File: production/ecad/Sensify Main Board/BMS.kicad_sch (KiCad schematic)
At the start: 0 parts

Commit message: rough draft for BMS schematic
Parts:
- added BT1, BT2: 3.7V, symbol Device:Battery_Cell
- added C1, C2, C3, C8: 0.47u, symbol Device:C
- added C10: 0.33u, symbol Device:C
- added C11: 10u, symbol Device:C_Polarized
- added C12: 470p, symbol Device:C
- added C13: 2.2u, symbol Device:C
- added C4, C6, C7: 0.01u, symbol Device:C
- added C5, C9: 0.1u, symbol Device:C
- added Q1, Q2, Q3: NMOS, symbol Simulation_SPICE:NMOS
- added R1: 5m, symbol Device:R_Shunt_US
- added R2: R_US, symbol Device:R_US
- added R3: 1k, symbol Device:R_US
- added R4, R5: 100, symbol Device:R_US
- added R6: 10k, symbol Device:R_US
- added R7, R8: 50, symbol Device:R_US
- added R9: 10, symbol Device:R_US
- added TH1: 10k, symbol Device:Thermistor_US
- added U1: MAX17320G22, MAX17320G22_:TQFN-24, symbol MAX17320G22_:MAX17320G22_
- added U2: LD29150DT33R, LD29150DT33R:DPAK456P972X240-3N, symbol LD29150DT33R:LD29150DT33R
- added U3: MIC5205-5.0YM5-TR, MIC5205-5.0YM5-TR:SOT95P280X145-5N, symbol MIC5205-5.0YM5-TR:MIC5205-5.0YM5-TR
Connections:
- new net: Q3.2 (G), R6.1, U1.11 (PFAIL)
- new net: C6.1, C7.2, R7.1, U1.21 (CELL1), U1.22 (CELL2), U1.23 (CELL3)
- new net: C5.1, Q1.1 (D)
- new net: C5.2, Q1.2 (G), R4.1
- new net: Q1.3 (S), Q2.1 (D)
- new net: C12.1, U3.4 (BYP)
- new net: C7.1, R8.1, U1.24 (BATTS)
- new net: R1.2, U1.15 (CSP)
- new net: R1.3, U1.14 (CSN)
- new net: R4.2, U1.3 (CHG)
- new net: BT1.2 (-), BT2.1 (+), R7.2
- new net: R2.2, U1.5 (ZVC)
- new net: TH1.2, U1.10 (TH1)
- new net: C1.1, U1.12 (AOLDO)
- new net: C3.1, U1.13 (REG3)
- new net: C2.1, U1.17 (REG2)
- new net: C8.1, U1.2 (CP)
- new net: R5.2, U1.4 (DIS)
- new net: C4.1, R3.2, U1.6 (PCKP)
- new net: U1.EP, U1.P$1 (EP), U1.P$2 (EP), U1.P$3 (EP), U1.P$4 (EP), U1.P$5 (EP)
- new net: Q2.2 (G), R5.1
- new net +3.3V: C11.1, U2.2 (OUTPUT)
- new net +5V: C13.1, U3.5 (OUT)
- new net GND: BT1.1 (+), BT2.2 (-), C1.2, C10.2, C11.2, C12.2, C13.2, C2.2, C3.2, C4.2, C6.2, C8.2, C9.1, C9.2, Q3.1 (D), R1.1, R6.2, R8.2, R9.1, R9.2, TH1.1, U1.1 (IN), U1.20 (GND), U2.3 (GND), U3.2 (GND)
- new net PACK+: C10.1, Q2.3 (S), R2.1, R3.1, U2.1 (INPUT), U3.1 (IN), U3.3 (EN)
- new net PACK-: R1.4
- new net SCL: U1.8 (SCL/OD)
- new net SDA: U1.9 (SDA/DQ)
- no-connect marks 0 -> 3
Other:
- note added: "3 terminal fuse"
- note added: "BMIC"
- note added: "Choose R"
- note added: "LDO (BATT->3.3V)"
- note added: "LDO (BATT->5V)"
- note added: "Tantalum"

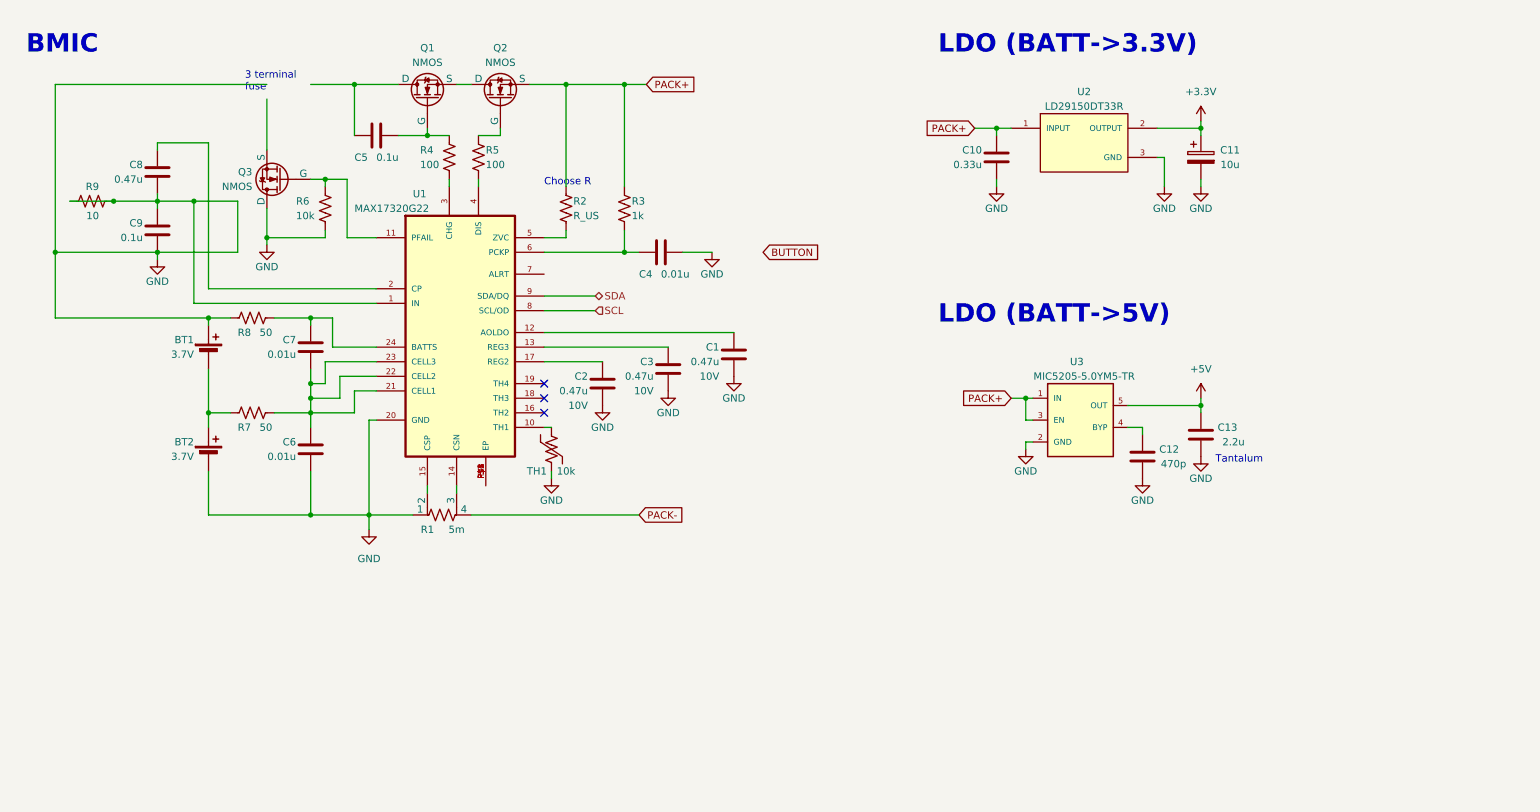
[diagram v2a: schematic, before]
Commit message: added to BMS schematic
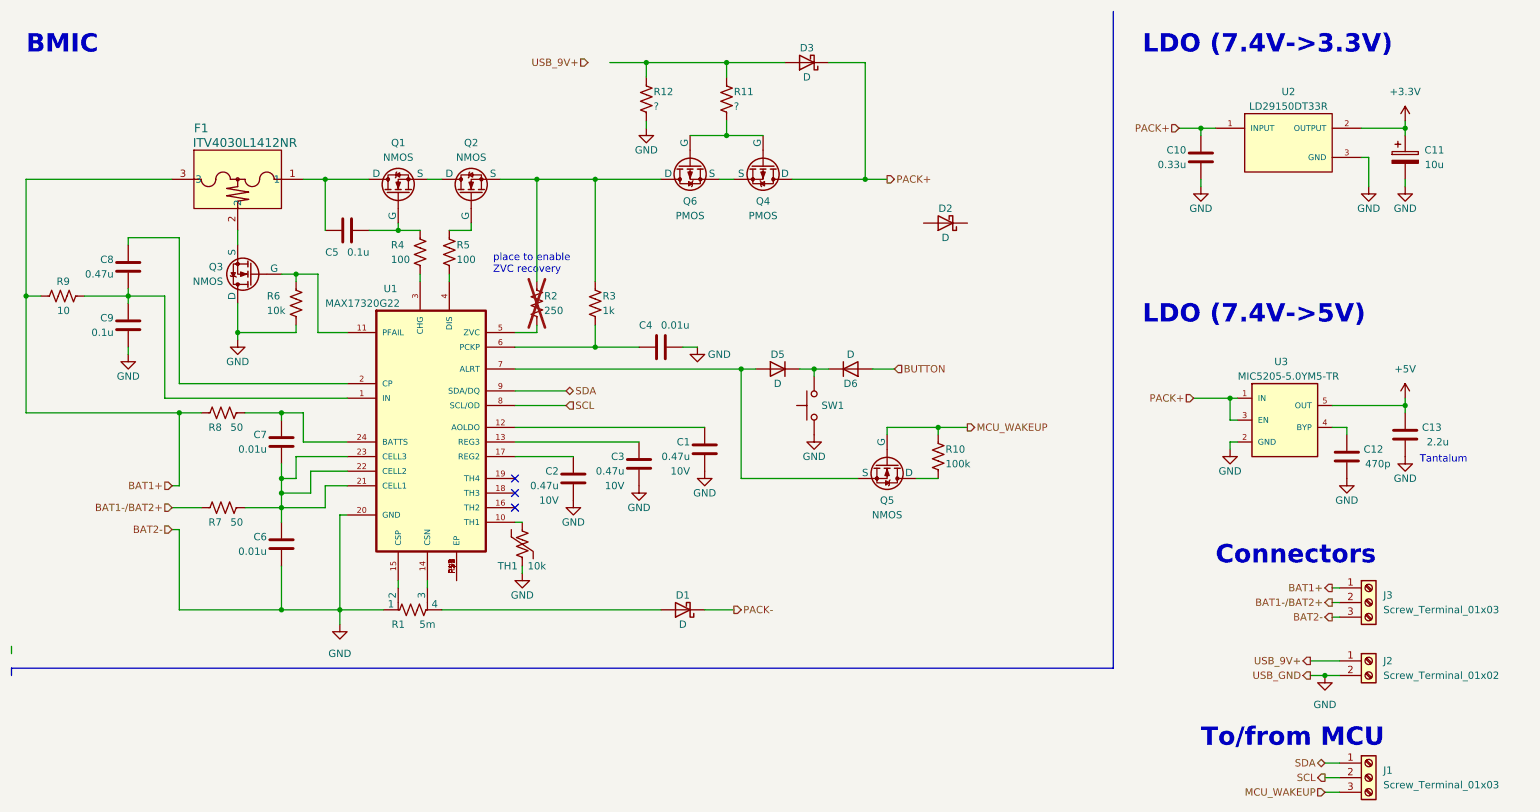
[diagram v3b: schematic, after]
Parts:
- removed BT1, BT2: 3.7V, symbol Device:Battery_Cell
- added D1, D2, D3: D, symbol Device:D_Schottky
- added D5, D6: D, symbol Device:D
- added F1: ITV4030L1412NR, BMS:ITV4030_LTF, symbol 2024-10-02_16-38-03:ITV4030L1412NR
- added J1, J3: Screw_Terminal_01x03, symbol Connector:Screw_Terminal_01x03
- added J2: Screw_Terminal_01x02, symbol Connector:Screw_Terminal_01x02
- added Q4, Q6: PMOS, symbol Simulation_SPICE:PMOS
- added Q5: NMOS, symbol Simulation_SPICE:NMOS
- added R10: 100k, symbol Device:R_US
- added R11, R12: ?, symbol Device:R_US
- added SW1: SW_Push, symbol Switch:SW_Push
- R2: value R_US -> 250; now not fitted
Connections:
- net BUTTON: now also D6.2 (A)
- net GND: now also J2.2 (Pin_2), J3.3 (Pin_3), R12.2, SW1.1; no longer C8.2, C9.1, R8.2, R9.1, R9.2, U1.1 (IN)
- net PACK+: now also D3.1 (K), Q4.1 (D); no longer Q2.3 (S), R2.1, R3.1
- net PACK-: now also D1.1 (K); no longer R1.4
- net SCL: now also J1.2 (Pin_2)
- net SDA: now also J1.1 (Pin_1)
- net at Q3.3 (S): now also F1.2
- net at C5.1, Q1.1 (D): now also F1.1
- net BAT1-/BAT2+: now reaches R7.2
- net BAT1-/BAT2+: now also J3.2 (Pin_2)
- net at U1.7 (ALRT): now also D5.2 (A), Q5.3 (S)
- new net: Q5.1 (D), R10.2
- new net: D5.1 (K), D6.1 (K), SW1.2
- new net: D1.2 (A), R1.4
- new net: D3.2 (A), R11.1, R12.1
- new net: C8.2, C9.1, R9.2, U1.1 (IN)
- new net: Q4.2 (G), Q6.2 (G), R11.2
- new net: Q2.3 (S), Q6.1 (D), R2.1, R3.1
- new net: Q4.3 (S), Q6.3 (S)
- new net BAT1+: F1.3, J3.1 (Pin_1), R8.2, R9.1
- new net MCU_WAKEUP: J1.3 (Pin_3), Q5.2 (G), R10.1
- new net USB_9V+: J2.1 (Pin_1)
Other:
- note added: "Connectors"
- note added: "LDO (7.4V->3.3V)"
- note added: "LDO (7.4V->5V)"
- note added: "To/from MCU"
- note added: "place to enable ZVC recovery"
- note removed: "3 terminal fuse"
- note removed: "Choose R"
- note removed: "LDO (BATT->3.3V)"
- note removed: "LDO (BATT->5V)"
- moved on the sheet: C1, C10, C11, C12, C13, C2, C3, C4, C5, C6, C7, C8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

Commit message: first draft of BMS schematic
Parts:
- removed C12: 470p, symbol Device:C
- removed C13: 2.2u, symbol Device:C
- removed D1, D2, D3: D, symbol Device:D_Schottky
- removed Q4, Q6: PMOS, symbol Simulation_SPICE:PMOS
- removed R11, R12: ?, symbol Device:R_US
- removed U3: MIC5205-5.0YM5-TR, MIC5205-5.0YM5-TR:SOT95P280X145-5N, symbol MIC5205-5.0YM5-TR:MIC5205-5.0YM5-TR
- added C14, C18, C28, C30: 10u, symbol Device:C
- added C15, C16: 2.2u, symbol Device:C
- added C17: 47n, symbol Device:C
- added C19: 470p, symbol Device:C
- added C29, C31, C32: 1u, symbol Device:C
- added C33, C35: 100n, symbol Device:C
- added C34: 18p, symbol Device:C
- added C36: 100u, symbol Device:C
- added D2: LED, symbol Device:LED
- added D4: D, symbol Device:D
- added L1: 2.2u, symbol Device:L
- added L3: 6.8u, symbol Device:L
- added Q8: PMOS, symbol Simulation_SPICE:PMOS
- added R13: 1k, symbol Device:R_US
- added R14: 33k, symbol Device:R_US
- added R15: 1.33M, symbol Device:R_US
- added R16: 200k, symbol Device:R_US
- added R17, R22, R25: 100k, symbol Device:R_US
- added R18: 4.7k, symbol Device:R_US
- added R19: 24.3k, symbol Device:R_US
- added R23: 24.9k, symbol Device:R_US
- added R24: 5k, symbol Device:R_US
- added TH2: 10k, symbol Device:Thermistor_US
- added U4: BQ25306RTER, BMS:IC_BQ25306RTER, symbol BMS:BQ25306RTER
- added U6: LM61480Q5RPHRQ1, BMS:RPH0016A, symbol BMS:LM61480Q5RPHRQ1
- U1: footprint MAX17320G22_:TQFN-24 -> BMS:TQFN-24
- U2: footprint LD29150DT33R:DPAK456P972X240-3N -> BMS:DPAK456P972X240-3N
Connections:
- net PACK+ is gone; now on net +5V: C10.1, U2.1 (INPUT)
- net +5V: now also C34.1, C35.1, C36.1, L3.2, R22.1, R25.1, U6.5 (BIAS)
- net BAT1+: now also Q2.3 (S), R2.1, R3.1, C18.1, C19.1, L1.2, Q8.1 (D), R15.1, R18.2, R19.1, TH2.2, U4.10 (BAT), U4.7 (TS)
- net GND: now also C14.1, C15.2, C16.2, C18.2, C28.2, C29.2, C30.2, C31.2, C32.2, C35.2, C36.2, R14.2, R17.2, R19.2, R23.2, TH2.1, U4.11 (GND), U4.12 (GND), U4.17 (EXP), U6.1 (PGND2), U6.11 (SpSp), U6.12 (SYNC_MODE), U6.15 (PGND1), U6.8 (AGND), U6.9 (RT)
- net PACK-: now also R1.4
- net USB_9V+: now also C16.1, D4.2 (A), U4.1 (VBUS)
- new net: C19.2, R15.2, R16.1, U4.9 (FB)
- new net: R16.2, U4.8 (FB_GND)
- new net: R22.2, R23.1, R24.2, U6.7 (FB)
- new net: R25.2, U6.10 (RESET)
- new net: D2.1 (K), R13.2
- new net: R13.1, U4.3 (STAT)
- new net: D4.1 (K), Q8.2 (G), R17.1
- new net: R14.1, U4.4 (ICHG)
- new net: C32.1, U6.6 (VCC)
- new net: C33.1, L3.1, U6.16 (SW)
- new net: C33.2, U6.3 (RBOOT), U6.4 (CBOOT)
- new net: C34.2, R24.1
- new net: C17.1, L1.1, U4.13 (SW), U4.14 (SW)
- new net: C17.2, U4.15 (BTST)
- new net REGN: C15.1, D2.2 (A), R18.1, U4.2 (REGN)
- new net SYSTEM_POWER: C14.2, C28.1, C29.1, C30.1, C31.1, Q8.3 (S), U4.16 (PMID), U6.13 (EN), U6.14 (VIN1), U6.2 (VIN2)
- no-connect marks 3 -> 5
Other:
- note added: "103AT-2"
- note added: "5V Buck"
- note added: "5V->3.3V LDO"
- note added: "9-8.4V->5V buck(3A) and 5V->3.3V LDO(1.5A)"
- note added: "9V @ 3A"
- note added: "Charge V = 1.1(1+1.33M/200k)"
- note added: "Charge current Ichg = 40k/RIchg ~1.2A = 40k/33k"
- note added: "Charger IC"
- note added: "Either from VBUS or batteries"
- note added: "External signals"
- note added: "Indicator LED"
- note added: "Power ground"
- note added: "Signal ground"
- note added: "Webench generated"
- note added: "place to enable ZVC recovery current"
- note added: "pulldown R unsure"
- note removed: "Connectors"
- note removed: "LDO (7.4V->3.3V)"
- note removed: "LDO (7.4V->5V)"
- note removed: "Tantalum"
- note removed: "place to enable ZVC recovery"
- moved on the sheet: C1, C2, C3, C4, C5, C6, C7, C8, C9, D5, D6, F1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

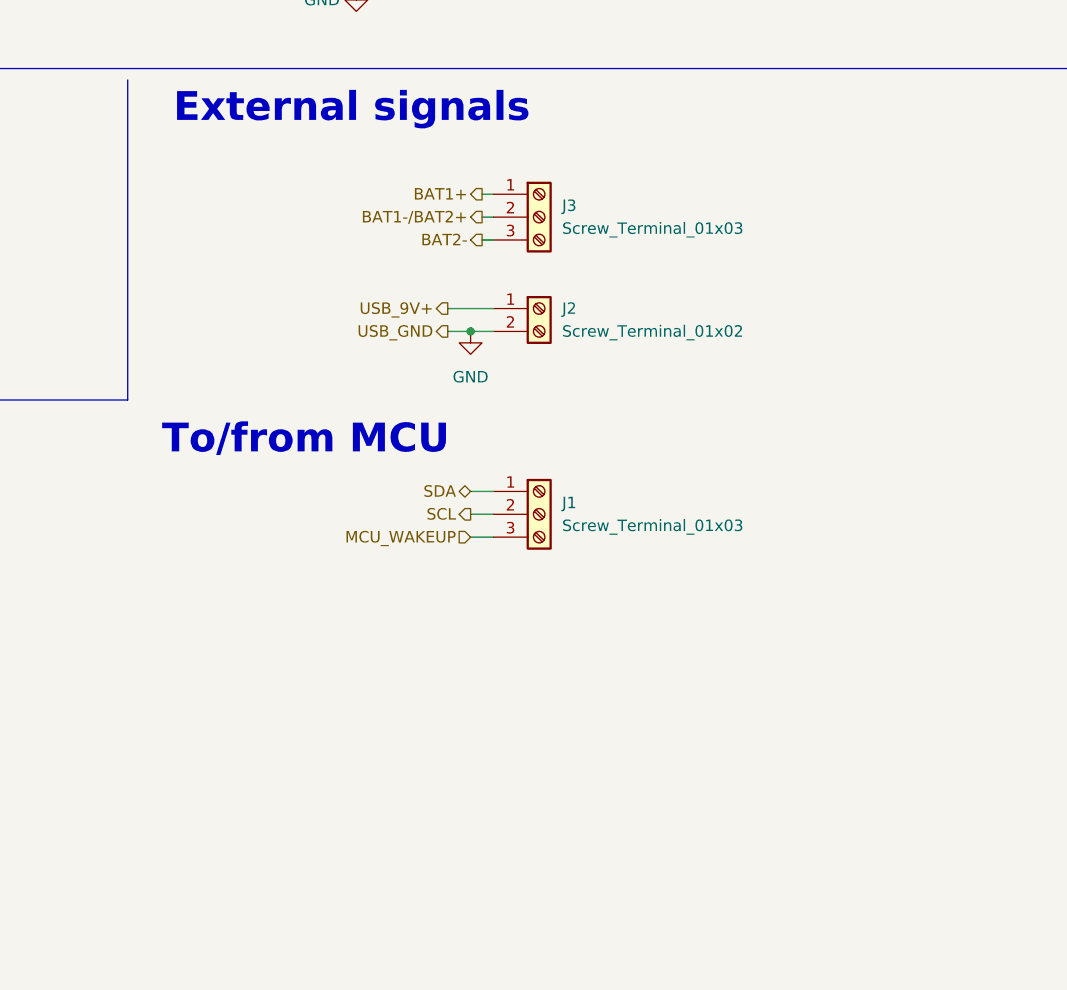
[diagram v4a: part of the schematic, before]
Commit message: added signals to other parts
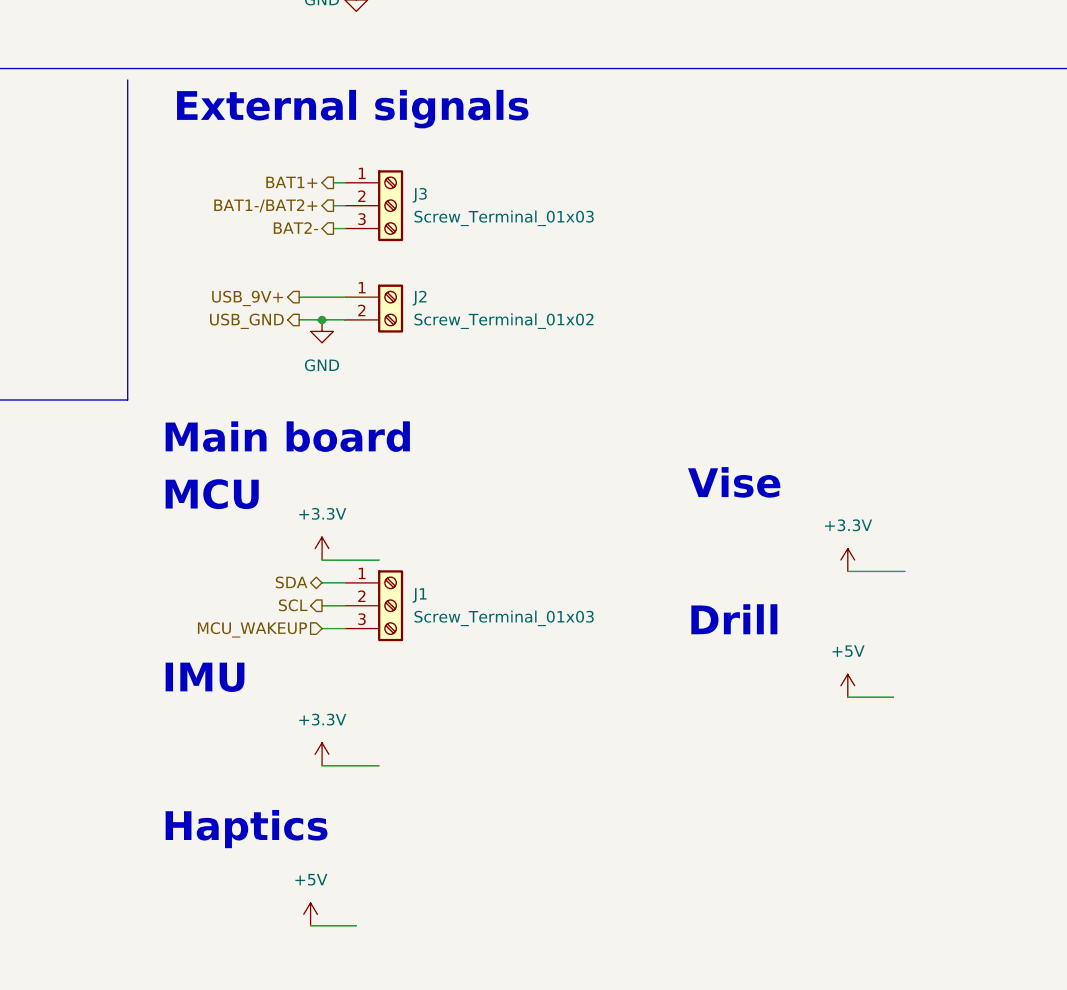
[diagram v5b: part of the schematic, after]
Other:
- note added: "Drill"
- note added: "Haptics"
- note added: "IMU"
- note added: "MCU"
- note added: "Main board"
- note added: "Vise"
- note removed: "To/from MCU"
- moved on the sheet: J1, J2, J3
